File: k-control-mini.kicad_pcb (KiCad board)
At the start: 2 copper layers, 59 x 89.1 mm, 87 parts, among them J1_P1 IN_L, J1_P2 IN_GND, J1_P3 IN_R, J1_P4 OUT_R, J1_P5 OUT_GND, J1_P6 OUT_L, J2_P1 HP_R, J2_P2 HP_GND, J2_P3 HP_L, U1 H11L1S(TA)

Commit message: thonk blue jacks
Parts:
- HEADPHONES1, MIDI-IN1, MIDI-OUT1, STEREO-IN1, STEREO-OUT1: value HC-PJ-320D-4P-S -> WQB729JH-B; footprint Connector_Audio:Jack_3.5mm_PJ320D_Horizontal -> Thonk:729JH-B
- moved R3 16.1 mm to (130.8, 86.6), turned to 90 degrees
- moved STEREO-IN1 10.7 mm to (129.4, 102.2)
- moved SW_PC1 10.6 mm to (137.7, 88.9)
- moved STEREO-OUT1 9.02 mm to (127.3, 115.8)
- moved R4 7.46 mm to (130.3, 74.2)
- moved SW_BP9 7.46 mm to (137.9, 69.8)
- moved MIDI-IN1 6.52 mm to (167.8, 104.3)
- moved MIDI-OUT1 4.10 mm to (168.1, 118.3)
- moved POT_PA1 0.74 mm to (144.3, 87.4)
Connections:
- R1 pad 2: Net-(MIDI-IN1-PadR1) -> Net-(MIDI-IN1-Pad2)
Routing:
- net +3.3V: track 96.6 -> 10.0 mm, vias 2 -> 0
- net PA0: track 57.6 -> 0.00 mm, vias 1 -> 0
- net Net-(D1-A): track 65.1 -> 10.1 mm
- net PA2: track 45.7 -> 0.00 mm, vias 3 -> 0
- net MO5: track 41.8 -> 0.00 mm
- net Net-(MIDI-IN1-PadR1): track 35.8 -> 0.00 mm
- net PA1: track 35.8 -> 0.00 mm, vias 3 -> 0
- net IN_L: track 30.6 -> 0.00 mm
- net IN_R: track 24.2 -> 0.00 mm, vias 2 -> 0
- net IN_GND: track 22.6 -> 0.00 mm, vias 2 -> 0
- net HP_GND: track 21.3 -> 0.00 mm
- net MO4: track 21.2 -> 0.00 mm
- net HP_L: track 14.9 -> 0.00 mm
- net HP_R: track 14.5 -> 0.00 mm
- net OUT_L: track 11.9 -> 0.00 mm
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
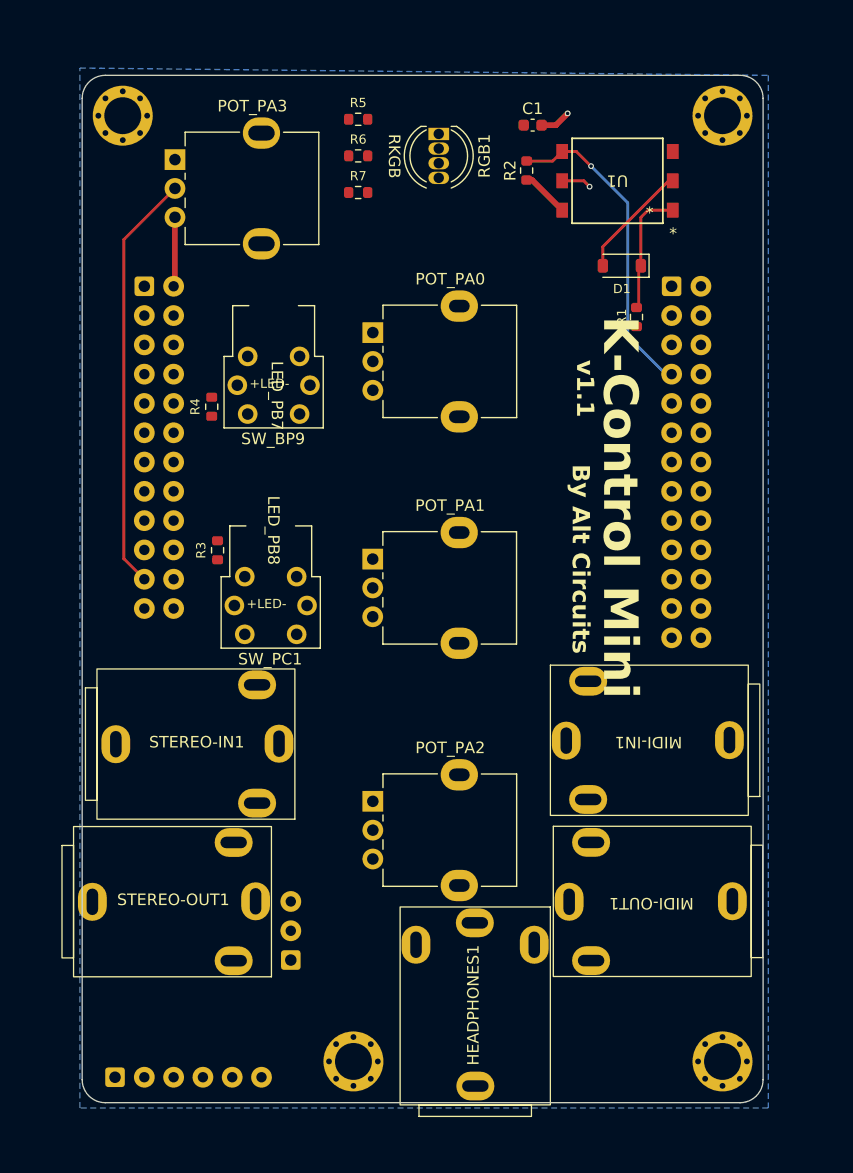
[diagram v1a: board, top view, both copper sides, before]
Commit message: footprint arangements
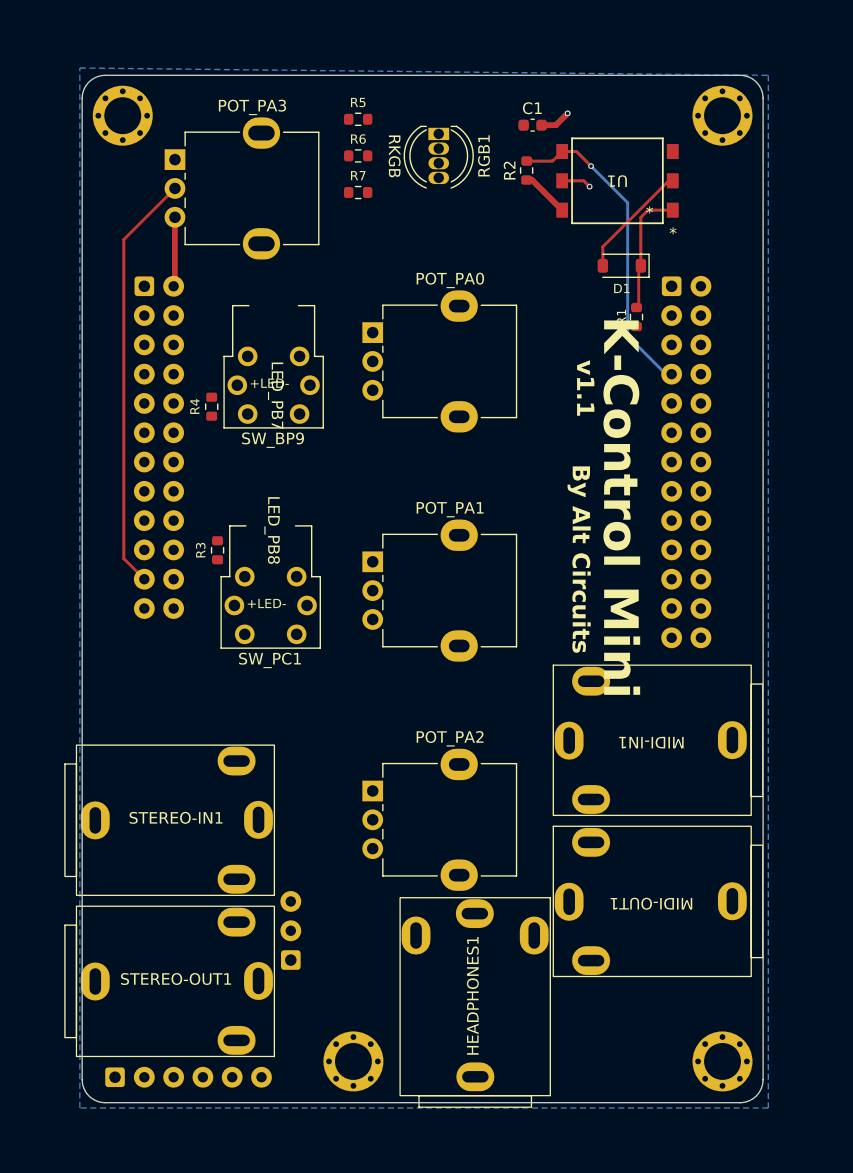
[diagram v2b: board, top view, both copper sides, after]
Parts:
- moved STEREO-OUT1 6.91 mm to (127.6, 122.7)
- moved STEREO-IN1 6.84 mm to (127.6, 108.8)
- moved POT_PA2 0.90 mm to (144.3, 107.5)
- moved HEADPHONES1 0.80 mm to (151.9, 124.9)
- moved MIDI-IN1 0.25 mm to (168.1, 104.3)
- moved POT_PA1 0.23 mm to (144.3, 87.6)
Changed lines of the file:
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@@
   )
   (footprint "Potentiometer_THT:Potentiometer_Alpha_RD901F-40-00D_Single_Vertical" (layer "F.Cu")
-    (at 144.266096 87.38)
+    (at 144.266096 87.615)
     (descr "Potentiometer, vertical, 9mm, single, http://www.taiwanalpha.com.tw/downloads?target=products&id=113")
     (tags "potentiometer vertical 9mm single")
@@
   )
   (footprint "Thonk:729JH-B" (layer "F.Cu")
-    (at 127.326096 115.828)
+    (at 127.580096 122.736)
     (property "Sheetfile" "k-control-mini.kicad_sch")
     (property "Sheetname" "")
@@
   )
   (footprint "Thonk:729JH-B" (layer "F.Cu")
-    (at 129.358096 102.162)
+    (at 127.580096 108.766)
     (property "Sheetfile" "k-control-mini.kicad_sch")
     (property "Sheetname" "")
@@
   )
   (footprint "Thonk:729JH-B" (layer "F.Cu")
-    (at 151.896096 125.703 90)
+    (at 151.896096 124.904 90)
     (property "Sheetfile" "k-control-mini.kicad_sch")
     (property "Sheetname" "")
@@
   )
   (footprint "Potentiometer_THT:Potentiometer_Alpha_RD901F-40-00D_Single_Vertical" (layer "F.Cu")
-    (at 144.276096 108.384)
+    (at 144.266096 107.486)
     (descr "Potentiometer, vertical, 9mm, single, http://www.taiwanalpha.com.tw/downloads?target=products&id=113")
     (tags "potentiometer vertical 9mm single")
@@
   )
   (footprint "Thonk:729JH-B" (layer "F.Cu")
-    (at 167.830096 104.348 180)
+    (at 168.084096 104.348 180)
     (property "Sheetfile" "k-control-mini.kicad_sch")
     (property "Sheetname" "")
@@
   )
   (footprint "Potentiometer_THT:Potentiometer_Alpha_RD901F-40-00D_Single_Vertical" (layer "F.Cu")
-    (at 144.276096 67.744)
+    (at 144.266096 67.744)
     (descr "Potentiometer, vertical, 9mm, single, http://www.taiwanalpha.com.tw/downloads?target=products&id=113")
     (tags "potentiometer vertical 9mm single")

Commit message: updated footprint locations for thonk jacks
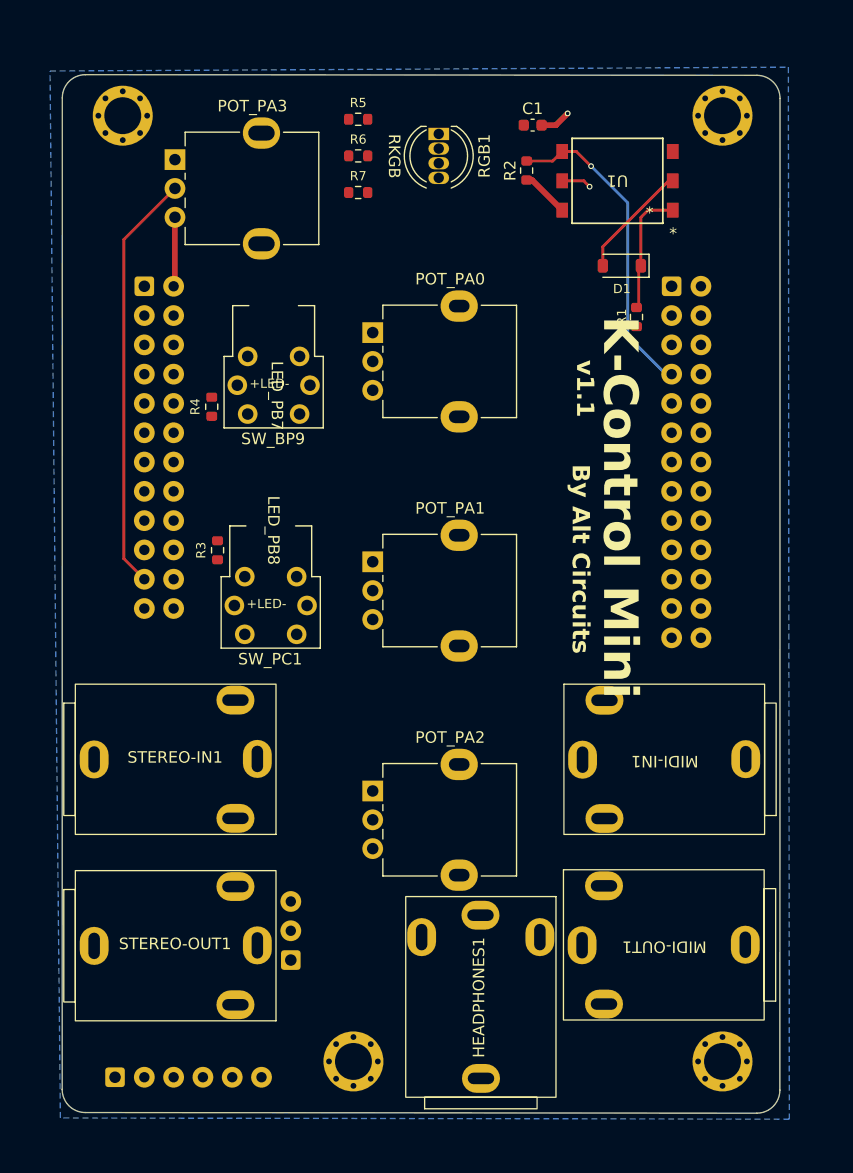
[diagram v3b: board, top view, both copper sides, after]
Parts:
- moved STEREO-IN1 5.28 mm to (127.5, 103.5)
- moved MIDI-OUT1 3.93 mm to (169.2, 122.1)
- moved STEREO-OUT1 3.09 mm to (127.5, 119.6)
- moved MIDI-IN1 2.02 mm to (169.2, 106.0)
- moved HEADPHONES1 0.51 mm to (152.4, 125.0)
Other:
- board size 59 x 89.1 mm -> 62.2 x 90 mm
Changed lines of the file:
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@@
   )
   (footprint "Thonk:729JH-B" (layer "F.Cu")
-    (at 168.084096 118.318 180)
+    (at 169.204096 122.088 180)
     (property "Sheetfile" "k-control-mini.kicad_sch")
     (property "Sheetname" "")
@@
     (fp_rect (start -10 -3.6175) (end -9 6.1325)
       (stroke (width 0.1) (type default)) (fill none) (layer "F.SilkS"))
-    (fp_rect (start 8.16 7.77) (end -9 -5.255)
+    (fp_rect (start 8.4 7.77) (end -9 -5.255)
       (stroke (width 0.1) (type default)) (fill none) (layer "F.SilkS"))
     (fp_rect (start 8.49 8.16) (end -10.15 -5.72)
@@
   )
   (footprint "Thonk:729JH-B" (layer "F.Cu")
-    (at 127.580096 122.736)
+    (at 127.480096 119.648)
     (property "Sheetfile" "k-control-mini.kicad_sch")
     (property "Sheetname" "")
@@
     (fp_rect (start -10 -3.6175) (end -9 6.1325)
       (stroke (width 0.1) (type default)) (fill none) (layer "F.SilkS"))
-    (fp_rect (start 8.16 7.77) (end -9 -5.255)
+    (fp_rect (start 8.4 7.77) (end -9 -5.255)
       (stroke (width 0.1) (type default)) (fill none) (layer "F.SilkS"))
     (fp_rect (start 8.49 8.16) (end -10.15 -5.72)
@@
   )
   (footprint "Thonk:729JH-B" (layer "F.Cu")
-    (at 127.580096 108.766)
+    (at 127.480096 103.483)
     (property "Sheetfile" "k-control-mini.kicad_sch")
     (property "Sheetname" "")
@@
     (fp_rect (start -10 -3.6175) (end -9 6.1325)
       (stroke (width 0.1) (type default)) (fill none) (layer "F.SilkS"))
-    (fp_rect (start 8.16 7.77) (end -9 -5.255)
+    (fp_rect (start 8.4 7.77) (end -9 -5.255)
       (stroke (width 0.1) (type default)) (fill none) (layer "F.SilkS"))
     (fp_rect (start 8.49 8.16) (end -10.15 -5.72)
@@
   )
   (footprint "Thonk:729JH-B" (layer "F.Cu")
-    (at 151.896096 124.904 90)
+    (at 152.384096 125.042 90)
     (property "Sheetfile" "k-control-mini.kicad_sch")
     (property "Sheetname" "")
@@
     (fp_rect (start -10 -3.6175) (end -9 6.1325)
       (stroke (width 0.1) (type default)) (fill none) (layer "F.SilkS"))
-    (fp_rect (start 8.16 7.77) (end -9 -5.255)
+    (fp_rect (start 8.4 7.77) (end -9 -5.255)
       (stroke (width 0.1) (type default)) (fill none) (layer "F.SilkS"))
     (fp_rect (start 8.49 8.16) (end -10.15 -5.72)
@@
   )
   (footprint "Thonk:729JH-B" (layer "F.Cu")
-    (at 168.084096 104.348 180)
+    (at 169.244096 105.998 180)
     (property "Sheetfile" "k-control-mini.kicad_sch")
     (property "Sheetname" "")
@@
     (fp_rect (start -10 -3.6175) (end -9 6.1325)
       (stroke (width 0.1) (type default)) (fill none) (layer "F.SilkS"))
-    (fp_rect (start 8.16 7.77) (end -9 -5.255)
+    (fp_rect (start 8.4 7.77) (end -9 -5.255)
       (stroke (width 0.1) (type default)) (fill none) (layer "F.SilkS"))
     (fp_rect (start 8.49 8.16) (end -10.15 -5.72)
@@
   (gr_line (start 158.024522 101.849085) (end 158.822441 101.849085)
     (stroke (width 0.370416) (type solid)) (layer "B.SilkS"))
-  (gr_arc (start 176.114096 45.437) (mid 177.528312 46.022785) (end 178.114096 47.437)
+  (gr_arc (start 177.582096 45.437) (mid 178.996312 46.022785) (end 179.582096 47.437)
     (stroke (width 0.1) (type default)) (layer "Edge.Cuts"))
-  (gr_line (start 176.114096 134.515) (end 121.074096 134.515)
+  (gr_line (start 177.569883 135.423788) (end 119.339883 135.367788)
     (stroke (width 0.1) (type default)) (layer "Edge.Cuts"))
-  (gr_line (start 121.074096 45.437) (end 176.114096 45.437)
+  (gr_line (start 119.352096 45.381) (end 177.582096 45.437)
     (stroke (width 0.1) (type default)) (layer "Edge.Cuts"))
-  (gr_line (start 178.114096 47.437) (end 178.114096 132.515)
+  (gr_line (start 179.582096 47.437) (end 179.569883 133.423788)
     (stroke (width 0.1) (type default)) (layer "Edge.Cuts"))
-  (gr_arc (start 178.114096 132.515) (mid 177.528309 133.929212) (end 176.114096 134.515)
+  (gr_arc (start 179.569883 133.423788) (mid 178.984096 134.838) (end 177.569883 135.423788)
     (stroke (width 0.1) (type default)) (layer "Edge.Cuts"))
-  (gr_line (start 119.074096 132.515) (end 119.074096 47.437)
+  (gr_line (start 117.339883 133.367788) (end 117.352096 47.381)
     (stroke (width 0.1) (type default)) (layer "Edge.Cuts"))
-  (gr_arc (start 121.074096 134.515) (mid 119.659885 133.929212) (end 119.074096 132.515)
+  (gr_arc (start 119.339883 135.367788) (mid 117.925672 134.782) (end 117.339883 133.367788)
     (stroke (width 0.1) (type default)) (layer "Edge.Cuts"))
-  (gr_arc (start 119.074096 47.437) (mid 119.659882 46.022785) (end 121.074096 45.437)
+  (gr_arc (start 117.352096 47.381) (mid 117.937882 45.966785) (end 119.352096 45.381)
     (stroke (width 0.1) (type default)) (layer "Edge.Cuts"))
   (gr_text "S1" (at 123.201096 73.918) (layer "B.SilkS")
@@
     (polygon
       (pts
-        (xy 178.566096 45.439)
-        (xy 178.566096 134.974)
-        (xy 118.876096 134.974)
-        (xy 118.876096 44.804)
+        (xy 180.306096 44.729)
+        (xy 180.386096 135.944)
+        (xy 117.184096 135.838)
+        (xy 116.286096 45.064)
       )
     )

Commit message: added thonk jacks model
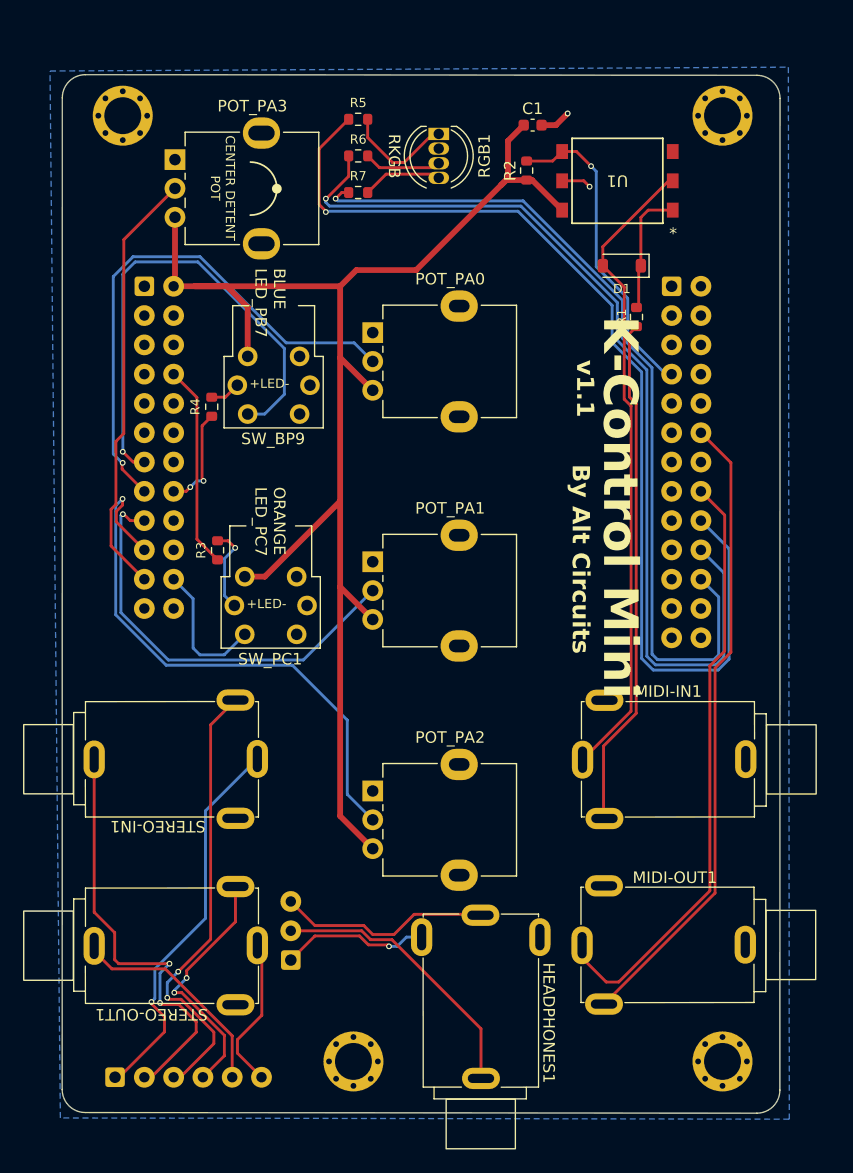
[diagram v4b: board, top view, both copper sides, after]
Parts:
- moved G513513 14.5 mm to (152.9, 109.4)
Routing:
- net +3.3V: track 10.0 -> 129.0 mm
- net PA4: track 0.00 -> 90.6 mm, vias 0 -> 1
- net PA5: track 0.00 -> 82.8 mm, vias 0 -> 1
- net PA6: track 0.00 -> 75.0 mm, vias 0 -> 1
- net MO4: track 0.00 -> 55.2 mm
- net MO5: track 0.00 -> 52.3 mm
- net PA2: track 0.00 -> 49.4 mm, vias 0 -> 1
- net PA0: track 0.00 -> 46.7 mm, vias 0 -> 1
- net Net-(D1-A): track 10.1 -> 55.7 mm
- net Net-(MIDI-IN1-Pad2): track 0.00 -> 44.4 mm
- net PA9: track 0.00 -> 43.0 mm, vias 0 -> 1
- net IN_R: track 0.00 -> 39.2 mm, vias 0 -> 2
- net IN_GND: track 0.00 -> 37.6 mm, vias 0 -> 2
- net PA1: track 0.00 -> 36.8 mm, vias 0 -> 1
- net IN_L: track 0.00 -> 33.9 mm, vias 0 -> 1
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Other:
- board text added: "BLUE LED_PB7"
- board text added: "CENTER DETENT POT"
- board text added: "ORANGE LED_PC7"
- board text removed: "LED_PB7"
- board text removed: "LED_PB8"

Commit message: rearranged board so audio jacks are on same side as USB
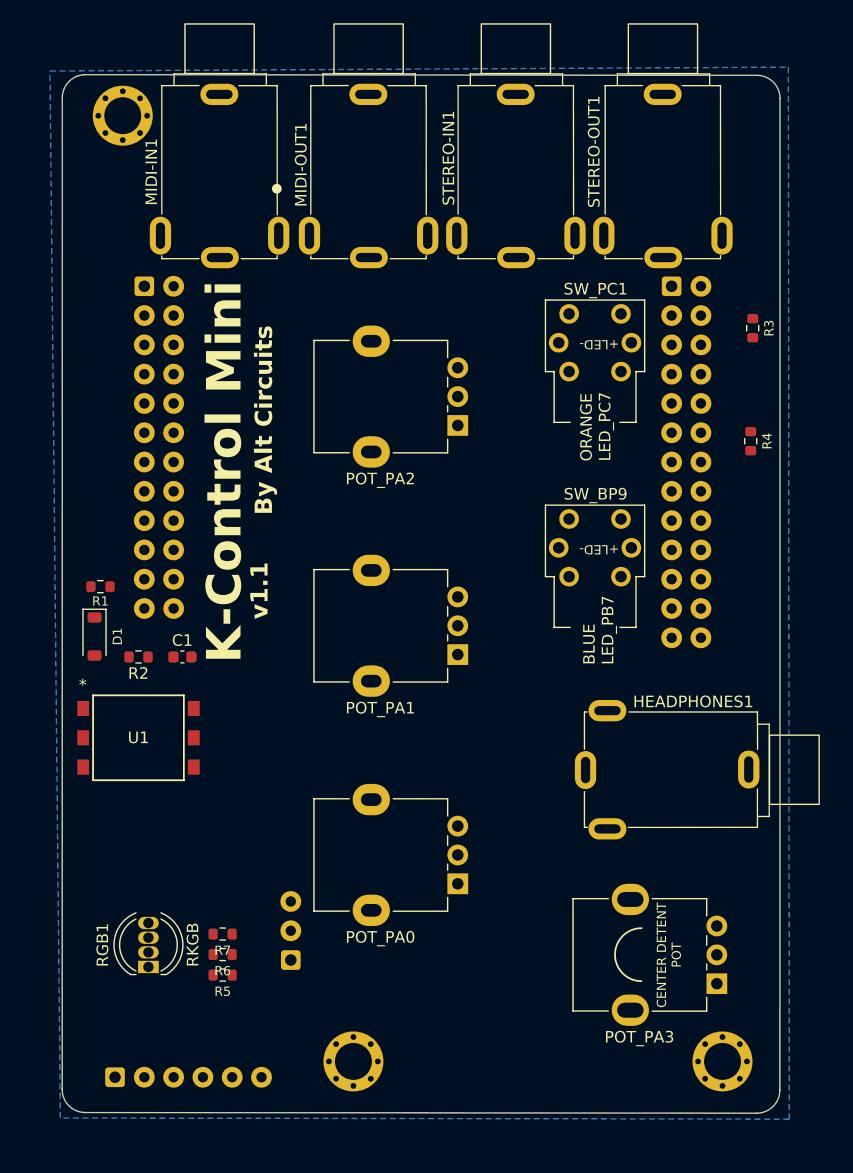
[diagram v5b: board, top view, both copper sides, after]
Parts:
- removed MH4: MountingHole, ksoloti_shield_footprints:MountingHole_3.2mm_M3_Pad_Via_tight
- moved POT_PA3 85.5 mm to (174.1, 124.2), turned to 180 degrees
- moved STEREO-OUT1 78.2 mm to (170.7, 54.5), turned to -90 degrees
- moved RGB1 76.5 mm to (124.8, 122.7), turned to 90 degrees
- moved R5 75.1 mm to (131.3, 123.4), turned to 180 degrees
- moved MIDI-OUT1 71.8 mm to (145.2, 54.5), turned to -90 degrees
- moved R6 70.2 mm to (131.3, 121.7), turned to 180 degrees
- moved R7 65.4 mm to (131.3, 119.9), turned to 180 degrees
- moved U1 63.7 mm to (124.0, 102.9), turned to 0 degrees
- moved MIDI-IN1 63.5 mm to (132.2, 54.5), turned to -90 degrees
- moved STEREO-IN1 57.7 mm to (157.9, 54.5), turned to -90 degrees
- moved D1 55.9 mm to (120.1, 94.1), turned to -90 degrees
- moved C1 55.2 mm to (127.8, 95.9)
- moved R2 54.0 mm to (124.0, 95.9), turned to 180 degrees
- moved R1 52.0 mm to (120.7, 89.8), turned to 0 degrees
- moved R3 50.2 mm to (177.2, 67.4), turned to -90 degrees
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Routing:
- net +3.3V: track 129.0 -> 0.00 mm
- net PA4: track 90.6 -> 0.00 mm, vias 1 -> 0
- net PA5: track 82.8 -> 0.00 mm, vias 1 -> 0
- net PA6: track 75.0 -> 0.00 mm, vias 1 -> 0
- net Net-(D1-A): track 55.7 -> 0.00 mm
- net MO4: track 55.2 -> 0.00 mm
- net MO5: track 52.3 -> 0.00 mm
- net PA2: track 49.4 -> 0.00 mm, vias 1 -> 0
- net PA0: track 46.7 -> 0.00 mm, vias 1 -> 0
- net Net-(MIDI-IN1-Pad2): track 44.4 -> 0.00 mm
- net PA9: track 43.0 -> 0.00 mm, vias 1 -> 0
- net IN_R: track 39.2 -> 0.00 mm, vias 2 -> 0
- net IN_GND: track 37.6 -> 0.00 mm, vias 2 -> 0
- net PA3: track 37.4 -> 0.00 mm
- net PA1: track 36.8 -> 0.00 mm, vias 1 -> 0
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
